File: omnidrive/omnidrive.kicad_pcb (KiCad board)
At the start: 2 copper layers, 76.2 x 25.4 mm, 77 parts, among them U1 TL072, U2 TL072

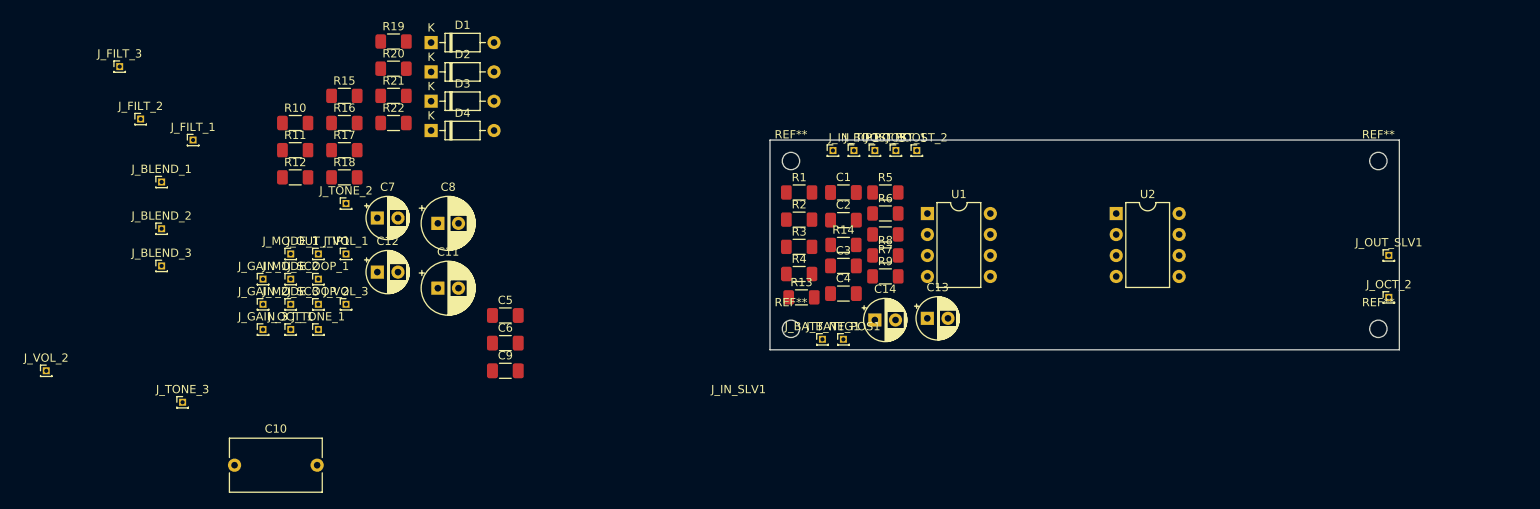
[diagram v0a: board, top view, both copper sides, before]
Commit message: more placement, attach output jack
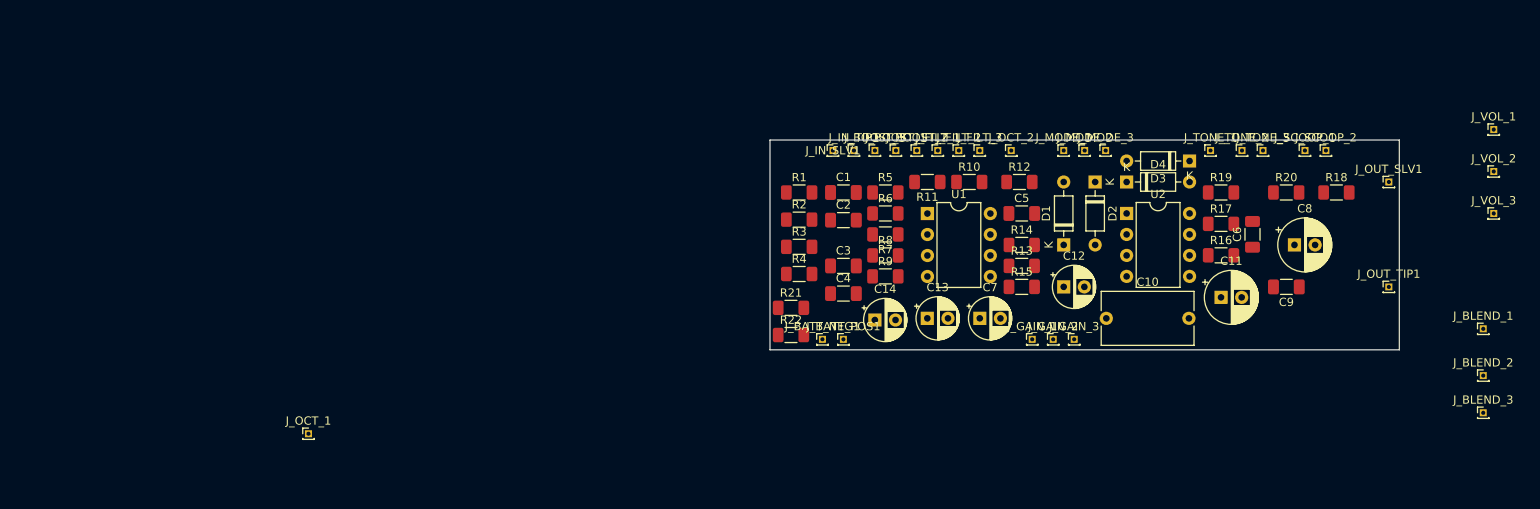
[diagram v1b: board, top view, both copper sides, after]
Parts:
- removed REF** (x4): MountingHole_2.1mm, MountingHole:MountingHole_2.1mm
- moved J_VOL_2 176.9 mm to (113.0, 29.2)
- moved J_BLEND_1 161.0 mm to (111.8, 48.3)
- moved J_BLEND_2 161.0 mm to (111.8, 53.9)
- moved J_BLEND_3 161.0 mm to (111.8, 58.4)
- moved J_VOL_1 139.8 mm to (113.0, 24.1)
- moved J_VOL_3 139.4 mm to (113.0, 34.3)
- moved J_TONE_3 134.3 mm to (85.1, 26.7)
- moved J_OUT_TIP1 129.7 mm to (100.3, 43.2)
- moved J_SCOOP_2 123.4 mm to (92.7, 26.7)
- moved J_SCOOP_1 120.5 mm to (90.2, 26.7)
- moved R18 120.1 mm to (94.0, 31.8)
- moved J_TONE_1 110.2 mm to (78.7, 26.7)
- moved R20 109.1 mm to (87.9, 31.8)
- moved J_TONE_2 108.7 mm to (82.5, 26.7)
- moved R16 107.3 mm to (80.0, 39.4)
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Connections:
- J_OUT_SLV1 pad 1: Net-(J_OUT_SLV1-Pin_1) -> GND
- J_OUT_TIP1 pad 1: Net-(J_OUT_TIP1-Pin_1) -> unconnected-(J_OUT_TIP1-Pin_1-Pad1)
- J_VOL_2 pad 1: Net-(J_OUT_TIP1-Pin_1) -> Net-(J_VOL_2-Pin_1)
- U2 pad 4: unconnected-(U2C-V--Pad4) -> GND
- U2 pad 8: unconnected-(U2C-V+-Pad8) -> /Vb

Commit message: fix some cnxs and place everything
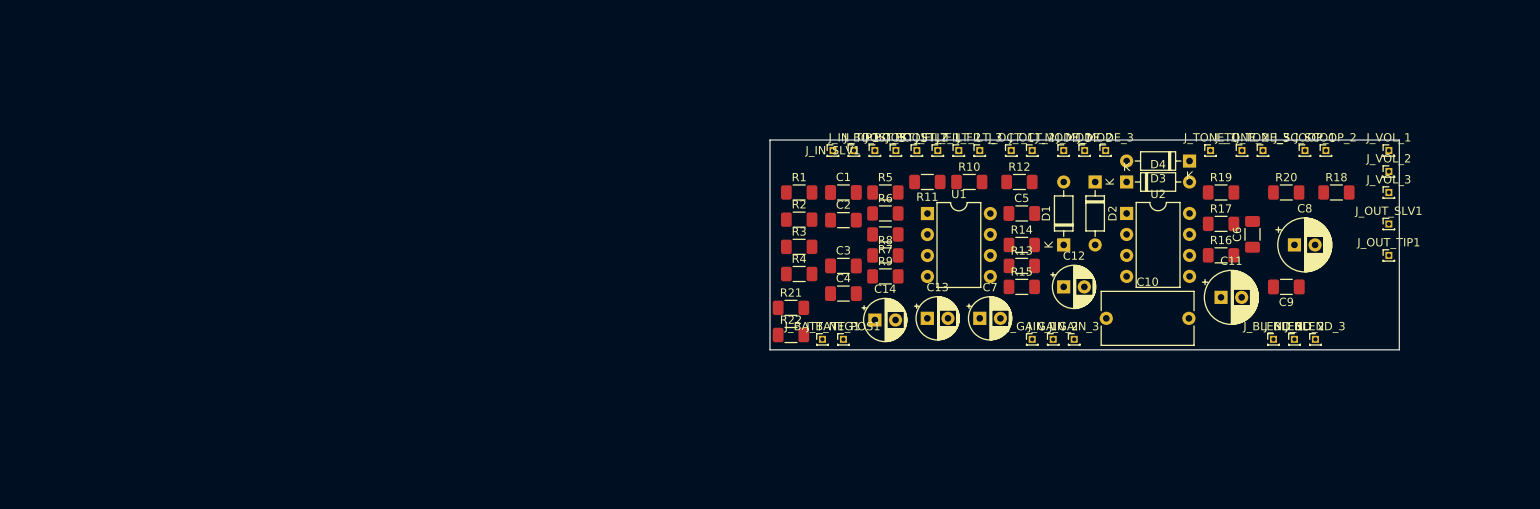
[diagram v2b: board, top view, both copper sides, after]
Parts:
- moved J_OCT_1 91.7 mm to (54.6, 26.7)
- moved J_BLEND_1 25.4 mm to (86.4, 49.5)
- moved J_BLEND_2 23.3 mm to (88.9, 49.5)
- moved J_BLEND_3 22.2 mm to (91.4, 49.5)
- moved J_VOL_1 13.0 mm to (100.3, 26.7)
- moved J_VOL_3 13.0 mm to (100.3, 31.8)
- moved J_VOL_2 12.7 mm to (100.3, 29.2)
- moved J_OUT_SLV1 5.08 mm to (100.3, 35.6)
- moved J_OUT_TIP1 3.81 mm to (100.3, 39.4)
- moved J_OCT_2 2.54 mm to (57.1, 26.7)
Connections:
- C5 pad 1: Net-(C5-Pad1) -> Net-(J_OCT_1-Pin_1)
- J_OCT_1 pad 1: unconnected-(J_OCT_1-Pin_1-Pad1) -> Net-(J_OCT_1-Pin_1)
- J_OUT_TIP1 pad 1: unconnected-(J_OUT_TIP1-Pin_1-Pad1) -> Net-(J_OUT_TIP1-Pin_1)
- J_VOL_2 pad 1: Net-(J_VOL_2-Pin_1) -> Net-(J_OUT_TIP1-Pin_1)
- R10 pad 1: Net-(C5-Pad1) -> Net-(J_OCT_1-Pin_1)

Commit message: some routing but not complete
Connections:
- U2 pad 1: unconnected-(U2-Pad1) -> Net-(D1-K)
- U2 pad 3: unconnected-(U2A-+-Pad3) -> /Vb
- U2 pad 8: /Vb -> +9V
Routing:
- net GND: track 0.00 -> 146.7 mm, vias 0 -> 4
- net /Vb: track 0.00 -> 91.4 mm, vias 0 -> 2
- net +9V: track 0.00 -> 78.7 mm, vias 0 -> 1
- net Net-(J_GAIN_1-Pin_1): track 0.00 -> 58.6 mm
- net Net-(J_FILT_2-Pin_1): track 0.00 -> 50.6 mm, vias 0 -> 1
- net Net-(J_TONE_1-Pin_1): track 0.00 -> 36.1 mm, vias 0 -> 1
- net Net-(J_GAIN_2-Pin_1): track 0.00 -> 34.7 mm
- net Net-(C7-Pad1): track 0.00 -> 34.1 mm
- net Net-(U2B-+): track 0.00 -> 33.2 mm
- net Net-(D2-K): track 0.00 -> 31.9 mm, vias 0 -> 2
- net Net-(J_FILT_1-Pin_1): track 0.00 -> 30.0 mm
- net Net-(J_OCT_1-Pin_1): track 0.00 -> 29.0 mm, vias 0 -> 1
- net Net-(U1B-+): track 0.00 -> 29.0 mm
- net Net-(J_TONE_2-Pin_1): track 0.00 -> 28.7 mm, vias 0 -> 2
- net Net-(J_BLEND_3-Pin_1): track 0.00 -> 28.3 mm
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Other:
- board size 76.2 x 25.4 mm -> 76.2 x 27.9 mm

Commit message: stuff
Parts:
- moved R4 4.53 mm to (24.4, 41.9)
- moved R1 4.52 mm to (24.4, 31.8)
- moved R2 4.52 mm to (24.4, 35.0)
- moved R3 4.52 mm to (24.4, 38.3)
- moved U1 1.27 mm to (43.2, 34.3)
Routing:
- net /Vb: track 91.4 -> 59.5 mm, vias 2 -> 0
- net Net-(U2B-+): track 33.2 -> 47.9 mm, vias 0 -> 1
- net Net-(J_OCT_1-Pin_1): track 29.0 -> 15.1 mm, vias 1 -> 2
- net Net-(J_BOOST_2-Pin_1): track 18.9 -> 30.7 mm
- net +9V: track 78.7 -> 69.5 mm, vias 1 -> 0
- net Net-(J_GAIN_1-Pin_1): track 58.6 -> 49.9 mm, vias 0 -> 1
- net GND: track 146.7 -> 155.0 mm, vias 4 -> 1
- net Net-(D1-A): track 26.9 -> 33.5 mm, vias 0 -> 1
- net Net-(C2-Pad2): track 12.3 -> 17.2 mm
- net Net-(D2-K): track 31.9 -> 27.2 mm, vias 2 -> 0
- net Net-(J_BOOST_3-Pin_1): track 17.0 -> 21.5 mm, vias 1 -> 0
- net Net-(C1-Pad2): track 12.4 -> 16.9 mm
- net Net-(U1A--): track 24.0 -> 28.6 mm, vias 2 -> 1
- net Net-(D1-K): track 12.6 -> 9.84 mm
- net Net-(J_FILT_1-Pin_1): track 30.0 -> 32.5 mm, vias 0 -> 1
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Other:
- board size 76.2 x 27.9 mm -> 96.5 x 38.1 mm
